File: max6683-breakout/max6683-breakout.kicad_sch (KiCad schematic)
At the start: 11 parts, among them J1 Conn_01x05, J2 Conn_01x05, U1 MAX6683

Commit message: Connect device address pin to GND
Supports #44.
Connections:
- net GND: now also JP3.1 (A); no longer JP3.3 (B)
- net SCL: now also JP2.1 (A); no longer JP2.3 (B)
- net SDA: now also JP3.3 (B); no longer JP3.1 (A)
- net at R4.2: now also JP2.3 (B); no longer JP2.1 (A)
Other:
- moved on the sheet: R4
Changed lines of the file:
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@@
+    (stroke (width 0) (type default) (color 0 0 0 0))
+  )
+  (wire (pts (xy 105.41 113.03) (xy 113.03 113.03))
     (stroke (width 0) (type default) (color 0 0 0 0))
   )
@@
     (stroke (width 0) (type default) (color 0 0 0 0))
   )
+  (wire (pts (xy 129.54 125.73) (xy 129.54 127))
+    (stroke (width 0) (type default) (color 0 0 0 0))
+  )
   (wire (pts (xy 171.45 57.15) (xy 171.45 59.69))
     (stroke (width 0) (type default) (color 0 0 0 0))
@@
     (stroke (width 0) (type default) (color 0 0 0 0))
   )
-  (wire (pts (xy 123.19 125.73) (xy 127 125.73))
-    (stroke (width 0) (type default) (color 0 0 0 0))
-  )
   (wire (pts (xy 171.45 81.28) (xy 173.99 81.28))
     (stroke (width 0) (type default) (color 0 0 0 0))
   )
-  (wire (pts (xy 110.49 127) (xy 110.49 125.73))
-    (stroke (width 0) (type default) (color 0 0 0 0))
-  )
   (wire (pts (xy 119.38 76.2) (xy 124.46 76.2))
     (stroke (width 0) (type default) (color 0 0 0 0))
@@
     (stroke (width 0) (type default) (color 0 0 0 0))
   )
+  (wire (pts (xy 123.19 125.73) (xy 129.54 125.73))
+    (stroke (width 0) (type default) (color 0 0 0 0))
+  )
   (wire (pts (xy 162.56 115.57) (xy 162.56 116.84))
     (stroke (width 0) (type default) (color 0 0 0 0))
   )
-  (wire (pts (xy 110.49 111.76) (xy 110.49 113.03))
+  (wire (pts (xy 129.54 111.76) (xy 129.54 113.03))
     (stroke (width 0) (type default) (color 0 0 0 0))
   )
@@
     (stroke (width 0) (type default) (color 0 0 0 0))
   )
-  (wire (pts (xy 123.19 113.03) (xy 127 113.03))
-    (stroke (width 0) (type default) (color 0 0 0 0))
-  )
   (wire (pts (xy 184.15 119.38) (xy 184.15 121.92))
     (stroke (width 0) (type default) (color 0 0 0 0))
   )
-  (wire (pts (xy 110.49 113.03) (xy 113.03 113.03))
+  (wire (pts (xy 123.19 113.03) (xy 129.54 113.03))
     (stroke (width 0) (type default) (color 0 0 0 0))
   )
@@
     (stroke (width 0) (type default) (color 0 0 0 0))
   )
-  (wire (pts (xy 110.49 125.73) (xy 113.03 125.73))
-    (stroke (width 0) (type default) (color 0 0 0 0))
-  )
   (wire (pts (xy 149.86 76.2) (xy 173.99 76.2))
     (stroke (width 0) (type default) (color 0 0 0 0))
@@
     (stroke (width 0) (type default) (color 0 0 0 0))
   )
-  (wire (pts (xy 110.49 102.87) (xy 110.49 104.14))
+  (wire (pts (xy 129.54 102.87) (xy 129.54 104.14))
+    (stroke (width 0) (type default) (color 0 0 0 0))
+  )
+  (wire (pts (xy 105.41 125.73) (xy 113.03 125.73))
     (stroke (width 0) (type default) (color 0 0 0 0))
   )
@@
     (effects (font (size 1.27 1.27)) (justify left bottom))
   )
-  (global_label "SCL" (shape input) (at 127 113.03 0) (fields_autoplaced)
-    (effects (font (size 1.27 1.27)) (justify left))
-    (property "Intersheet References" "${INTERSHEET_REFS}" (id 0) (at 132.8318 112.9506 0)
-      (effects (font (size 1.27 1.27)) (justify left) hide)
-    )
-  )
-  (global_label "SDA" (shape input) (at 127 125.73 0) (fields_autoplaced)
-    (effects (font (size 1.27 1.27)) (justify left))
-    (property "Intersheet References" "${INTERSHEET_REFS}" (id 0) (at 132.8923 125.6506 0)
-      (effects (font (size 1.27 1.27)) (justify left) hide)
+  (global_label "SCL" (shape input) (at 105.41 113.03 180) (fields_autoplaced)
+    (effects (font (size 1.27 1.27)) (justify right))
+    (property "Intersheet References" "${INTERSHEET_REFS}" (id 0) (at 99.5782 113.1094 0)
+      (effects (font (size 1.27 1.27)) (justify right) hide)
+    )
+  )
+  (global_label "SDA" (shape input) (at 105.41 125.73 180) (fields_autoplaced)
+    (effects (font (size 1.27 1.27)) (justify right))
+    (property "Intersheet References" "${INTERSHEET_REFS}" (id 0) (at 99.5177 125.8094 0)
+      (effects (font (size 1.27 1.27)) (justify right) hide)
     )
   )
@@
     (pin "5")
   )
-  (symbol (lib_id "power:GND") (at 110.49 127 0) (unit 1)
-    (in_bom no) (on_board yes)
-    (property "Reference" "#PWR0104" (id 0) (at 110.49 133.35 0)
-      (effects (font (size 1.27 1.27)) hide)
-    )
-    (property "Value" "" (id 1) (at 110.617 131.3942 0))
-    (property "Footprint" "" (id 2) (at 110.49 127 0)
-      (effects (font (size 1.27 1.27)) hide)
-    )
-    (property "Datasheet" "" (id 3) (at 110.49 127 0)
+  (symbol (lib_id "power:GND") (at 129.54 127 0) (unit 1)
+    (in_bom no) (on_board yes)
+    (property "Reference" "#PWR0104" (id 0) (at 129.54 133.35 0)
+      (effects (font (size 1.27 1.27)) hide)
+    )
+    (property "Value" "" (id 1) (at 129.667 131.3942 0))
+    (property "Footprint" "" (id 2) (at 129.54 127 0)
+      (effects (font (size 1.27 1.27)) hide)
+    )
+    (property "Datasheet" "" (id 3) (at 129.54 127 0)
       (effects (font (size 1.27 1.27)) hide)
     )
@@
     (pin "1")
   )
-  (symbol (lib_id "power:+3.3V") (at 110.49 102.87 0) (unit 1)
-    (in_bom no) (on_board yes)
-    (property "Reference" "#PWR0108" (id 0) (at 110.49 106.68 0)
-      (effects (font (size 1.27 1.27)) hide)
-    )
-    (property "Value" "" (id 1) (at 110.871 98.4758 0))
-    (property "Footprint" "" (id 2) (at 110.49 102.87 0)
-      (effects (font (size 1.27 1.27)) hide)
-    )
-    (property "Datasheet" "" (id 3) (at 110.49 102.87 0)
+  (symbol (lib_id "power:+3.3V") (at 129.54 102.87 0) (unit 1)
+    (in_bom no) (on_board yes)
+    (property "Reference" "#PWR0108" (id 0) (at 129.54 106.68 0)
+      (effects (font (size 1.27 1.27)) hide)
+    )
+    (property "Value" "" (id 1) (at 129.921 98.4758 0))
+    (property "Footprint" "" (id 2) (at 129.54 102.87 0)
+      (effects (font (size 1.27 1.27)) hide)
+    )
+    (property "Datasheet" "" (id 3) (at 129.54 102.87 0)
       (effects (font (size 1.27 1.27)) hide)
     )
@@
     (pin "2")
   )
-  (symbol (lib_id "Device:R_US") (at 110.49 107.95 0) (unit 1)
-    (in_bom yes) (on_board yes)
-    (property "Reference" "R4" (id 0) (at 112.2172 106.7816 0)
-      (effects (font (size 1.27 1.27)) (justify left))
-    )
-    (property "Value" "10k" (id 1) (at 112.2172 109.093 0)
-      (effects (font (size 1.27 1.27)) (justify left))
-    )
-    (property "Footprint" "Resistor_SMD:R_0603_1608Metric" (id 2) (at 111.506 108.204 90)
-      (effects (font (size 1.27 1.27)) hide)
-    )
-    (property "Datasheet" "https://industrial.panasonic.com/cdbs/www-data/pdf/RDA0000/AOA0000C304.pdf" (id 3) (at 110.49 107.95 0)
-      (effects (font (size 1.27 1.27)) hide)
-    )
-    (property "Part Number" "ERJ-3EKF1002V" (id 4) (at 110.49 107.95 0)
-      (effects (font (size 1.27 1.27)) hide)
-    )
-    (property "Manufacturer" "Panasonic" (id 5) (at 110.49 107.95 0)
-      (effects (font (size 1.27 1.27)) hide)
-    )
+  (symbol (lib_id "Device:R_US") (at 129.54 107.95 0) (unit 1)
+    (in_bom yes) (on_board yes)
+    (property "Reference" "R4" (id 0) (at 131.2672 106.7816 0)
+      (effects (font (size 1.27 1.27)) (justify left))
+    )
+    (property "Value" "10k" (id 1) (at 131.2672 109.093 0)
+      (effects (font (size 1.27 1.27)) (justify left))
+    )
+    (property "Footprint" "Resistor_SMD:R_0603_1608Metric" (id 2) (at 130.556 108.204 90)
+      (effects (font (size 1.27 1.27)) hide)
+    )
+    (property "Datasheet" "https://industrial.panasonic.com/cdbs/www-data/pdf/RDA0000/AOA0000C304.pdf" (id 3) (at 129.54 107.95 0)
+      (effects (font (size 1.27 1.27)) hide)
+    )
+    (property "Part Number" "ERJ-3EKF1002V" (id 4) (at 129.54 107.95 0)
+      (effects (font (size 1.27 1.27)) hide)
+    )
+    (property "Manufacturer" "Panasonic" (id 5) (at 129.54 107.95 0)
+      (effects (font (size 1.27 1.27)) hide)
+    )

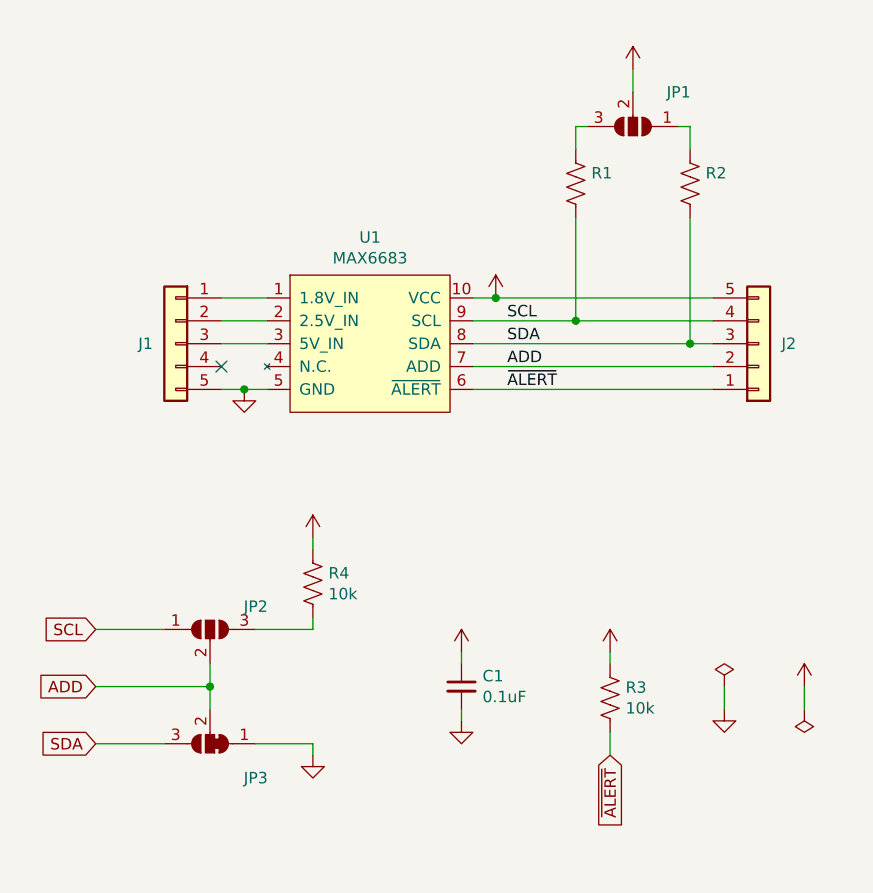
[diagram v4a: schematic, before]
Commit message: Add NC solder jumper to ALERT net
Supports #44.
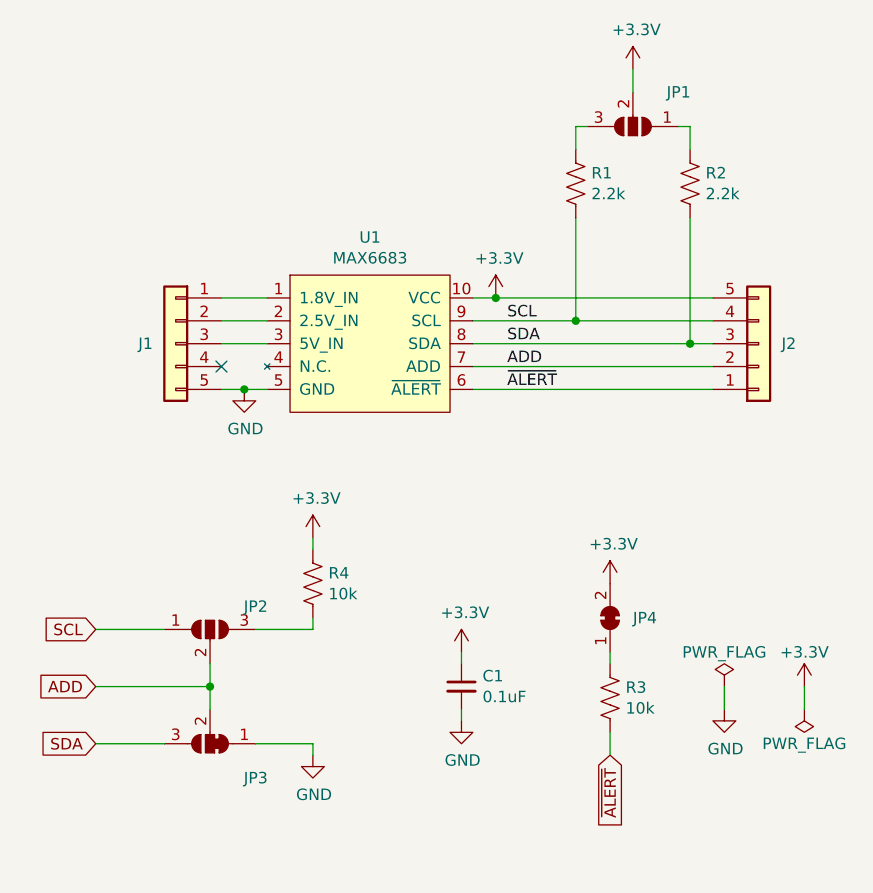
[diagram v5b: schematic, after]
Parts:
- added JP4: (no value), symbol Jumper:SolderJumper_2_Bridged
- JP1, JP2: value (none) -> SolderJumper_3_Open; footprint (none) -> Jumper:SolderJumper-3_P1.3mm_Open_RoundedPad1.0x1.5mm
- JP3: value (none) -> SolderJumper_3_Bridged12; footprint (none) -> Jumper:SolderJumper-3_P1.3mm_Bridged12_RoundedPad1.0x1.5mm
- R1, R2: value (none) -> 2.2k; footprint (none) -> Resistor_SMD:R_0603_1608Metric
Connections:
- net +3V3: now also JP4.2 (B); no longer R3.1
- new net: JP4.1 (A), R3.1
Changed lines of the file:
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@@
       (effects (font (size 1.27 1.27)) (justify left))
     )
-    (property "Value" "" (id 1) (at 160.4772 64.643 0)
-      (effects (font (size 1.27 1.27)) (justify left))
-    )
-    (property "Footprint" "" (id 2) (at 159.766 63.754 90)
+    (property "Value" "2.2k" (id 1) (at 160.4772 64.643 0)
+      (effects (font (size 1.27 1.27)) (justify left))
+    )
+    (property "Footprint" "Resistor_SMD:R_0603_1608Metric" (id 2) (at 159.766 63.754 90)
       (effects (font (size 1.27 1.27)) hide)
     )
@@
       (effects (font (size 1.27 1.27)) hide)
     )
-    (property "Value" "" (id 1) (at 165.481 46.4058 0))
+    (property "Value" "+3.3V" (id 1) (at 165.481 46.4058 0))
     (property "Footprint" "" (id 2) (at 165.1 50.8 0)
       (effects (font (size 1.27 1.27)) hide)
@@
       (effects (font (size 1.27 1.27)) hide)
     )
-    (property "Value" "" (id 1) (at 150.241 71.8058 0))
+    (property "Value" "+3.3V" (id 1) (at 150.241 71.8058 0))
     (property "Footprint" "" (id 2) (at 149.86 76.2 0)
       (effects (font (size 1.27 1.27)) hide)
@@
       (effects (font (size 1.27 1.27)) hide)
     )
-    (property "Value" "" (id 1) (at 122.047 90.7542 0))
+    (property "Value" "GND" (id 1) (at 122.047 90.7542 0))
     (property "Footprint" "" (id 2) (at 121.92 86.36 0)
       (effects (font (size 1.27 1.27)) hide)
@@
       (effects (font (size 1.27 1.27)) hide)
     )
-    (property "Value" "" (id 1) (at 129.667 131.3942 0))
+    (property "Value" "GND" (id 1) (at 129.667 131.3942 0))
     (property "Footprint" "" (id 2) (at 129.54 127 0)
       (effects (font (size 1.27 1.27)) hide)
@@
       (effects (font (size 1.27 1.27)) hide)
     )
-    (property "Value" "" (id 1) (at 146.431 111.1758 0))
+    (property "Value" "+3.3V" (id 1) (at 146.431 111.1758 0))
     (property "Footprint" "" (id 2) (at 146.05 115.57 0)
       (effects (font (size 1.27 1.27)) hide)
@@
       (effects (font (size 1.27 1.27)) hide)
     )
-    (property "Value" "" (id 1) (at 146.177 127.5842 0))
+    (property "Value" "GND" (id 1) (at 146.177 127.5842 0))
     (property "Footprint" "" (id 2) (at 146.05 123.19 0)
       (effects (font (size 1.27 1.27)) hide)
@@
     (pin "1")
   )
-  (symbol (lib_id "power:+3.3V") (at 162.56 115.57 0) (unit 1)
-    (in_bom no) (on_board yes)
-    (property "Reference" "#PWR0107" (id 0) (at 162.56 119.38 0)
-      (effects (font (size 1.27 1.27)) hide)
-    )
-    (property "Value" "" (id 1) (at 162.941 111.1758 0))
-    (property "Footprint" "" (id 2) (at 162.56 115.57 0)
-      (effects (font (size 1.27 1.27)) hide)
-    )
-    (property "Datasheet" "" (id 3) (at 162.56 115.57 0)
+  (symbol (lib_id "power:+3.3V") (at 162.56 107.95 0) (unit 1)
+    (in_bom no) (on_board yes)
+    (property "Reference" "#PWR0107" (id 0) (at 162.56 111.76 0)
+      (effects (font (size 1.27 1.27)) hide)
+    )
+    (property "Value" "+3.3V" (id 1) (at 162.941 103.5558 0))
+    (property "Footprint" "" (id 2) (at 162.56 107.95 0)
+      (effects (font (size 1.27 1.27)) hide)
+    )
+    (property "Datasheet" "" (id 3) (at 162.56 107.95 0)
       (effects (font (size 1.27 1.27)) hide)
     )
@@
       (effects (font (size 1.27 1.27)) hide)
     )
-    (property "Value" "" (id 1) (at 129.921 98.4758 0))
+    (property "Value" "+3.3V" (id 1) (at 129.921 98.4758 0))
     (property "Footprint" "" (id 2) (at 129.54 102.87 0)
       (effects (font (size 1.27 1.27)) hide)
@@
       (effects (font (size 1.27 1.27)) (justify left))
     )
-    (property "Value" "" (id 1) (at 173.1772 64.643 0)
-      (effects (font (size 1.27 1.27)) (justify left))
-    )
-    (property "Footprint" "" (id 2) (at 172.466 63.754 90)
+    (property "Value" "2.2k" (id 1) (at 173.1772 64.643 0)
+      (effects (font (size 1.27 1.27)) (justify left))
+    )
+    (property "Footprint" "Resistor_SMD:R_0603_1608Metric" (id 2) (at 172.466 63.754 90)
       (effects (font (size 1.27 1.27)) hide)
     )
@@
     (in_bom no) (on_board yes)
     (property "Reference" "JP3" (id 0) (at 123.19 129.54 0))
-    (property "Value" "" (id 1) (at 118.11 129.54 0)
-      (effects (font (size 1.27 1.27)) hide)
-    )
-    (property "Footprint" "" (id 2) (at 118.11 125.73 0)
+    (property "Value" "SolderJumper_3_Bridged12" (id 1) (at 118.11 129.54 0)
+      (effects (font (size 1.27 1.27)) hide)
+    )
+    (property "Footprint" "Jumper:SolderJumper-3_P1.3mm_Bridged12_RoundedPad1.0x1.5mm" (id 2) (at 118.11 125.73 0)
       (effects (font (size 1.27 1.27)) hide)
     )
@@
     (pin "3")
   )
+  (symbol (lib_id "Jumper:SolderJumper_2_Bridged") (at 162.56 111.76 90) (unit 1)
+    (in_bom no) (on_board yes) (fields_autoplaced)
+    (property "Reference" "JP4" (id 0) (at 165.1 111.7599 90)
+      (effects (font (size 1.27 1.27)) (justify right))
+    )
+    (property "Value" "" (id 1) (at 158.75 111.76 0)
+      (effects (font (size 1.27 1.27)) hide)
+    )
+    (property "Footprint" "" (id 2) (at 162.56 111.76 0)
+      (effects (font (size 1.27 1.27)) hide)
+    )
+    (property "Datasheet" "~" (id 3) (at 162.56 111.76 0)
+      (effects (font (size 1.27 1.27)) hide)
+    )
+    (pin "1")
+    (pin "2")
+  )
   (symbol (lib_id "power:GND") (at 175.26 121.92 0) (unit 1)
     (in_bom no) (on_board yes)
@@
       (effects (font (size 1.27 1.27)) hide)
     )
-    (property "Value" "" (id 1) (at 175.387 126.3142 0))
+    (property "Value" "GND" (id 1) (at 175.387 126.3142 0))
     (property "Footprint" "" (id 2) (at 175.26 121.92 0)
       (effects (font (size 1.27 1.27)) hide)
@@
       (effects (font (size 1.27 1.27)) hide)
     )
-    (property "Value" "" (id 1) (at 184.15 115.57 0))
+    (property "Value" "+3.3V" (id 1) (at 184.15 115.57 0))
     (property "Footprint" "" (id 2) (at 184.15 119.38 0)
       (effects (font (size 1.27 1.27)) hide)
@@
       (effects (font (size 1.27 1.27)) hide)
     )
-    (property "Value" "" (id 1) (at 175.26 115.57 0))
+    (property "Value" "PWR_FLAG" (id 1) (at 175.26 115.57 0))
     (property "Footprint" "" (id 2) (at 175.26 119.38 0)
       (effects (font (size 1.27 1.27)) hide)
@@
       (effects (font (size 1.27 1.27)) hide)
     )
-    (property "Value" "" (id 1) (at 184.15 125.73 0))
+    (property "Value" "PWR_FLAG" (id 1) (at 184.15 125.73 0))
     (property "Footprint" "" (id 2) (at 184.15 121.92 0)
       (effects (font (size 1.27 1.27)) hide)
@@
     (in_bom no) (on_board yes)
     (property "Reference" "JP2" (id 0) (at 123.19 110.49 0))
-    (property "Value" "" (id 1) (at 118.11 109.22 0)
-      (effects (font (size 1.27 1.27)) hide)
-    )
-    (property "Footprint" "" (id 2) (at 118.11 113.03 0)
+    (property "Value" "SolderJumper_3_Open" (id 1) (at 118.11 109.22 0)
+      (effects (font (size 1.27 1.27)) hide)
+    )
+    (property "Footprint" "Jumper:SolderJumper-3_P1.3mm_Open_RoundedPad1.0x1.5mm" (id 2) (at 118.11 113.03 0)
       (effects (font (size 1.27 1.27)) hide)
     )
@@
     (in_bom no) (on_board yes)
     (property "Reference" "JP1" (id 0) (at 170.18 53.34 0))
-    (property "Value" "" (id 1) (at 165.1 63.5 0)
-      (effects (font (size 1.27 1.27)) hide)
-    )
-    (property "Footprint" "" (id 2) (at 165.1 57.15 0)
+    (property "Value" "SolderJumper_3_Open" (id 1) (at 165.1 63.5 0)
+      (effects (font (size 1.27 1.27)) hide)
+    )
+    (property "Footprint" "Jumper:SolderJumper-3_P1.3mm_Open_RoundedPad1.0x1.5mm" (id 2) (at 165.1 57.15 0)
       (effects (font (size 1.27 1.27)) hide)
     )
@@
       (reference "JP3") (unit 1) (value "SolderJumper_3_Bridged12") (footprint "Jumper:SolderJumper-3_P1.3mm_Bridged12_RoundedPad1.0x1.5mm")
     )
+    (path "/18b6dcb6-5ab3-481b-b998-33e8cf6d281f"
+      (reference "JP4") (unit 1) (value "SolderJumper_2_Bridged") (footprint "")
+    )
     (path "/00000000-0000-0000-0000-00006201c9d1"
